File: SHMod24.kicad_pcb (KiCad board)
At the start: 2 copper layers, 49.5 x 49.5 mm, 63 parts, among them IC1 ArduinoProMini, J1 Conn_02x14_Odd_Even, J2 Conn_01x01, J3 Conn_01x01, J4 RESET, J5 12V, J6 GND, J9 Screw_Terminal_01x02, Q1 FS8205A, Q2 AO3400A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

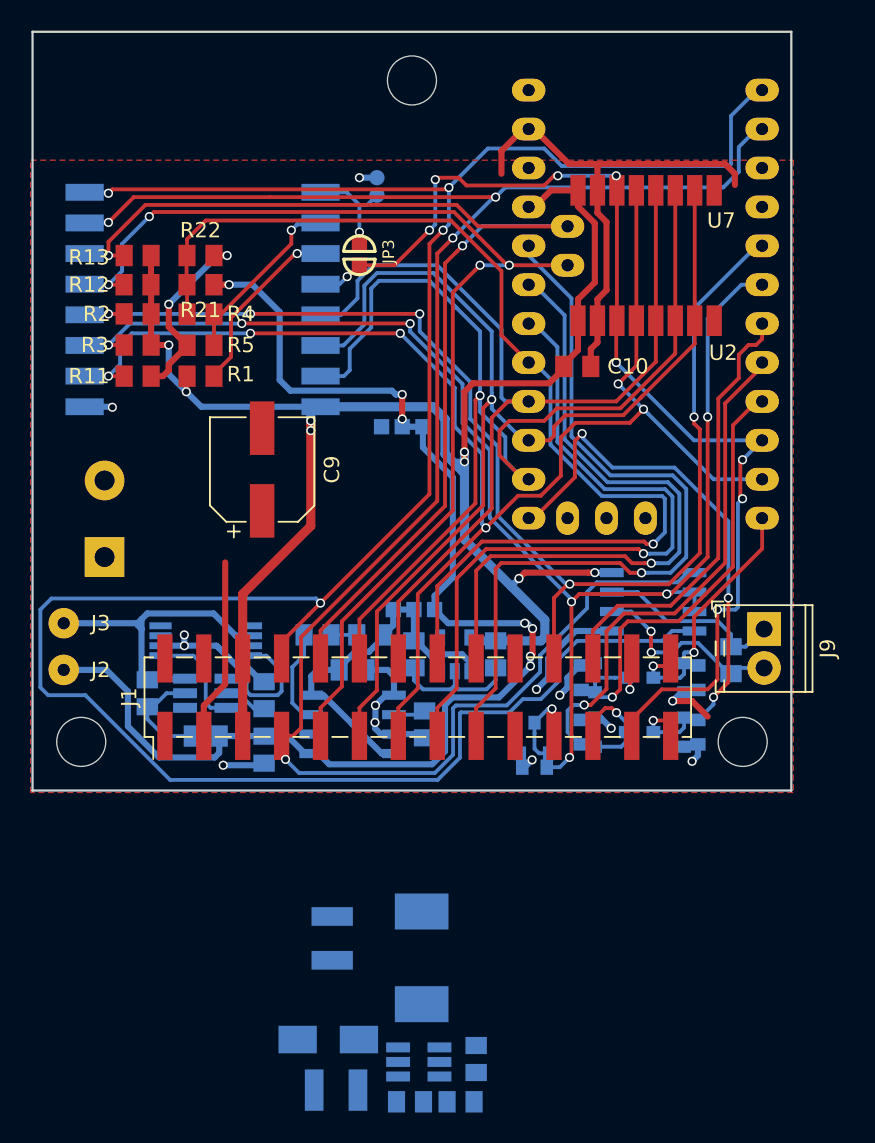
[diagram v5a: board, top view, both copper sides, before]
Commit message: fix switching regulator layout
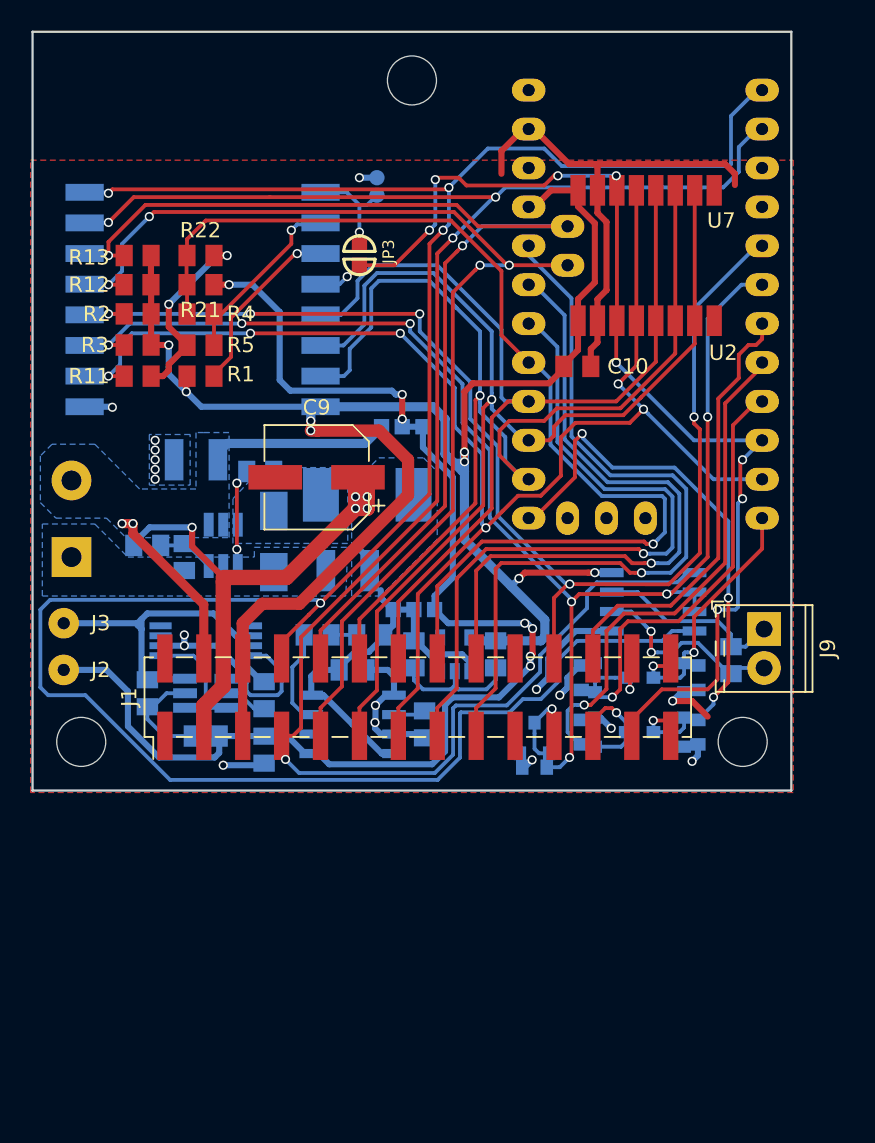
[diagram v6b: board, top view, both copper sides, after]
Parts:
- moved C7 42.2 mm to (61.5, 90.2)
- moved R9 41.7 mm to (58.3, 95.8), turned to 0 degrees
- moved C6 40.9 mm to (65.7, 90.9), turned to 0 degrees
- moved R10 38.5 mm to (60.7, 96.5), turned to 270 degrees
- moved U6 36.1 mm to (63.2, 95.8), turned to 90 degrees
- moved D1 32.7 mm to (66.5, 95.5), turned to 270 degrees
- moved L1 30.4 mm to (72.6, 92.5), turned to 0 degrees
- moved C8 24.0 mm to (71.4, 97.4), turned to 180 degrees
- moved C9 3.59 mm to (69.3, 91.3), turned to 180 degrees
- moved J5 2.16 mm to (53.3, 96.5)
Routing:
- net +5V: track 38.1 -> 65.3 mm, vias 0 -> 5
- net VCC: track 0.00 -> 23.3 mm, vias 0 -> 2
- net +3V3: track 112.8 -> 121.4 mm
- net Net-(C6-Pad1): track 0.00 -> 6.47 mm, vias 0 -> 2
- net Net-(R10-Pad1): track 0.00 -> 3.79 mm
- net GND: vias 15 -> 20
- added copper zone on B.Cu, net +5V
- added copper zone on B.Cu, net /SW
- added copper zone on B.Cu, net GND
- added copper zone on B.Cu, net VCC

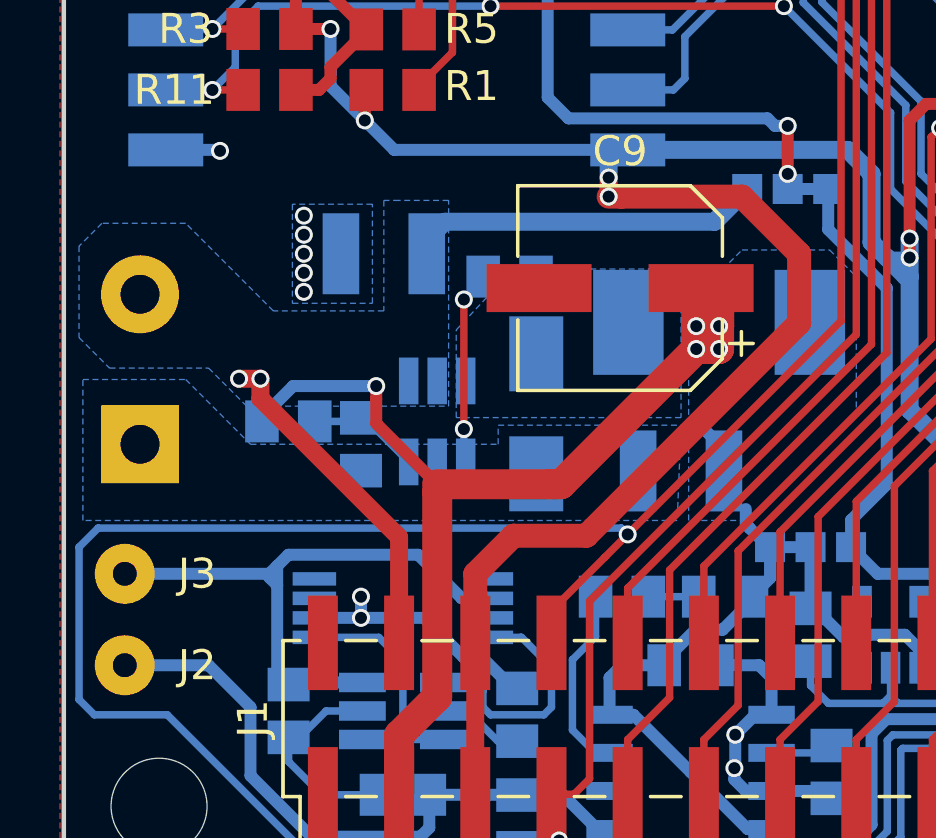
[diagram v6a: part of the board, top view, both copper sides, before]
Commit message: improve switching regulator capacitor placement
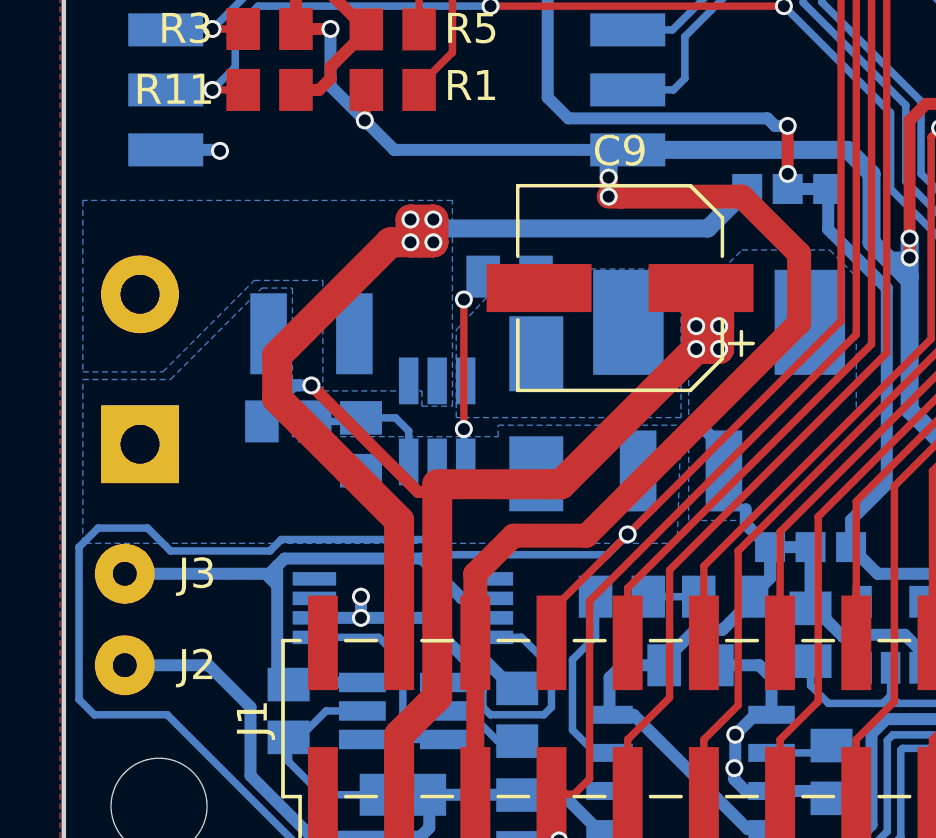
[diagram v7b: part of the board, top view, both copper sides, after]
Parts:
- moved C7 3.60 mm to (59.1, 92.8)
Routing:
- net VCC: track 23.3 -> 32.2 mm, vias 2 -> 4
- net TX: track 160.0 -> 160.9 mm
- net Net-(R10-Pad1): track 3.79 -> 4.39 mm
- net +5V: track 65.3 -> 64.7 mm
- net GND: vias 20 -> 15

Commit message: add power LED && place references better
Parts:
- added D3: LED, LED_SMD:LED_0805_2012Metric, B.Cu at (73.3, 84.6)
- added R23: 1k, Resistor_SMD:R_0805_2012Metric, B.Cu at (76.6, 84.6)
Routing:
- net +3V3: track 121.4 -> 124.6 mm
- net GPIO13: track 77.7 -> 74.6 mm
- net GPIO12: track 74.6 -> 71.8 mm
- net GPIO14: track 65.3 -> 63.4 mm
- net CS: track 94.0 -> 95.7 mm
- net Net-(D3-Pad2): track 0.00 -> 1.54 mm
- net GPIO2: track 98.0 -> 99.4 mm
- net SCL: track 72.5 -> 71.1 mm
- net GPIO0: track 81.0 -> 82.1 mm
- net SDA: track 73.2 -> 72.1 mm
- net TX: track 160.9 -> 162.0 mm
- net GND: track 91.4 -> 92.5 mm, vias 15 -> 16
- net RX: track 126.4 -> 125.8 mm
